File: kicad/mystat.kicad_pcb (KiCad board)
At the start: 2 copper layers, 80 x 80 mm, 66 parts, among them K1 9007-05-01, K2 9007-05-01, K3 9007-05-01, K4 9007-05-01, P1 USB Terminal, P2 CELL, P3 ICSP, U1 LM2662, U2 PIC16F1459, U3 ADR421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

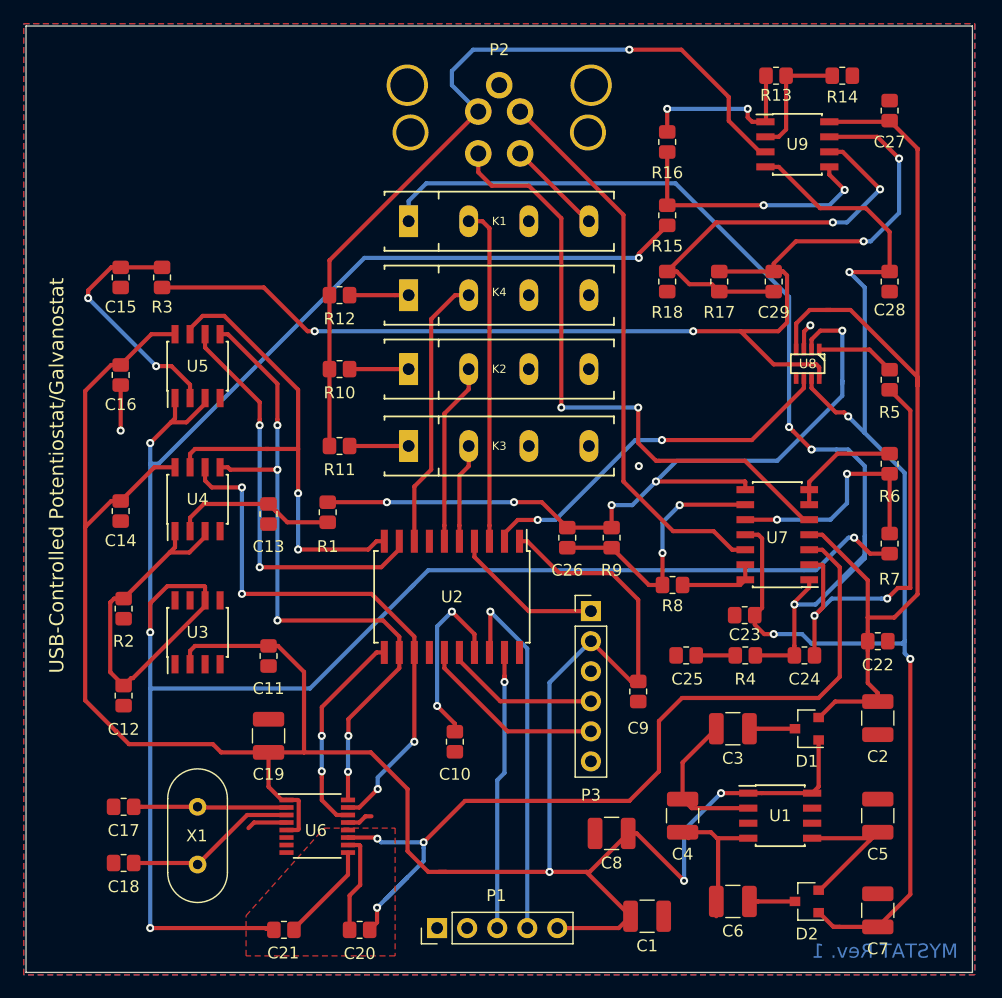
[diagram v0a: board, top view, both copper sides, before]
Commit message: Add files via upload
Modified PCB layout.  Made overall PCB dimensions smaller to fit the chosen case, all traces were made as wide as possible, changed relative position of all components in an attempt to minimize overall trace length.
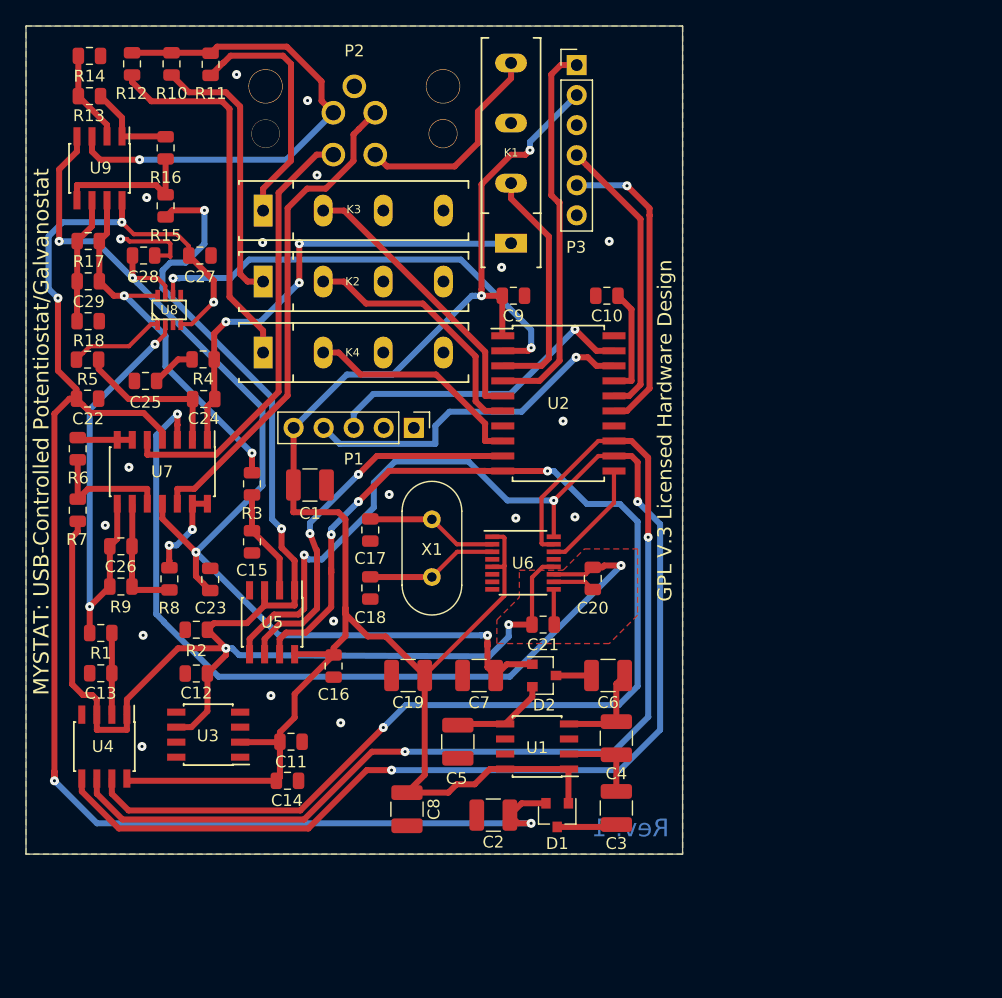
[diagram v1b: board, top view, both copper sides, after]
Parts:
- moved C22 69.9 mm to (55.2, 81.5)
- moved R7 68.7 mm to (54.4, 90.9)
- moved R6 68.6 mm to (54.4, 85.7)
- moved R5 67.8 mm to (55.2, 78.2), turned to 180 degrees
- moved R14 63.7 mm to (55.4, 52.5)
- moved C28 63.1 mm to (59.9, 69.4), turned to 0 degrees
- moved C27 59.6 mm to (64.7, 69.4), turned to 180 degrees
- moved U9 59.0 mm to (56.2, 62.0), turned to 270 degrees
- moved R13 58.1 mm to (55.4, 55.9), turned to 0 degrees
- moved C29 57.9 mm to (55.3, 71.6), turned to 0 degrees
- moved C24 55.2 mm to (65.0, 81.5), turned to 180 degrees
- moved U8 54.2 mm to (62.1, 74.0), turned to 90 degrees
- moved R17 53.4 mm to (55.3, 68.2), turned to 0 degrees
- moved U7 52.3 mm to (61.5, 87.7), turned to 270 degrees
- moved R4 52.2 mm to (65.0, 78.2)
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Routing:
- net /VREF: track 220.4 -> 134.4 mm, vias 5 -> 4
- net /SCK: track 58.0 -> 128.9 mm, vias 5 -> 4
- net /I_MEAS: track 97.6 -> 32.0 mm, vias 4 -> 2
- net /CS2: track 44.4 -> 108.0 mm, vias 2 -> 4
- net +5V: track 215.6 -> 157.2 mm, vias 3 -> 2
- net Net-(C24-Pad1): track 87.7 -> 39.5 mm
- net /SDIO: track 46.8 -> 90.8 mm, vias 4 -> 2
- net +9V: track 90.3 -> 129.8 mm, vias 0 -> 5
- net /V_MEAS: track 67.9 -> 38.4 mm, vias 5 -> 2
- net Net-(K4-Pad1): track 4.99 -> 31.6 mm
- net /CE: track 69.8 -> 44.2 mm
- net Net-(C29-Pad1): track 36.2 -> 10.7 mm, vias 2 -> 0
- net Net-(C24-Pad2): track 35.6 -> 13.3 mm, vias 2 -> 0
- net /MCLR: track 13.1 -> 32.5 mm
- net Net-(K2-Pad1): track 4.99 -> 23.3 mm
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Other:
- board size 80 x 80 mm -> 55.5 x 70 mm
- net class Default: clearance 0.2286 -> 0.254; trace_width 0.2286 -> 0.508; via_dia 0.6858 -> 0.762; via_drill 0.3302 -> 0.254
- net class power removed
- rule trace_clearance: 0.2286 -> 0.254
- board text added: "GPL V.3 Licensed Hardware Design"
- board text added: "MYSTAT: USB-Controlled Potentiostat/Galvanostat"
- board text added: "Rev. 1"
- board text removed: "MYSTAT Rev. 1"
- board text removed: "USB-Controlled Potentiostat/Galvanostat"

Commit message: Add files via upload
Corrected PCB trace routing to provide more direct ground return paths.
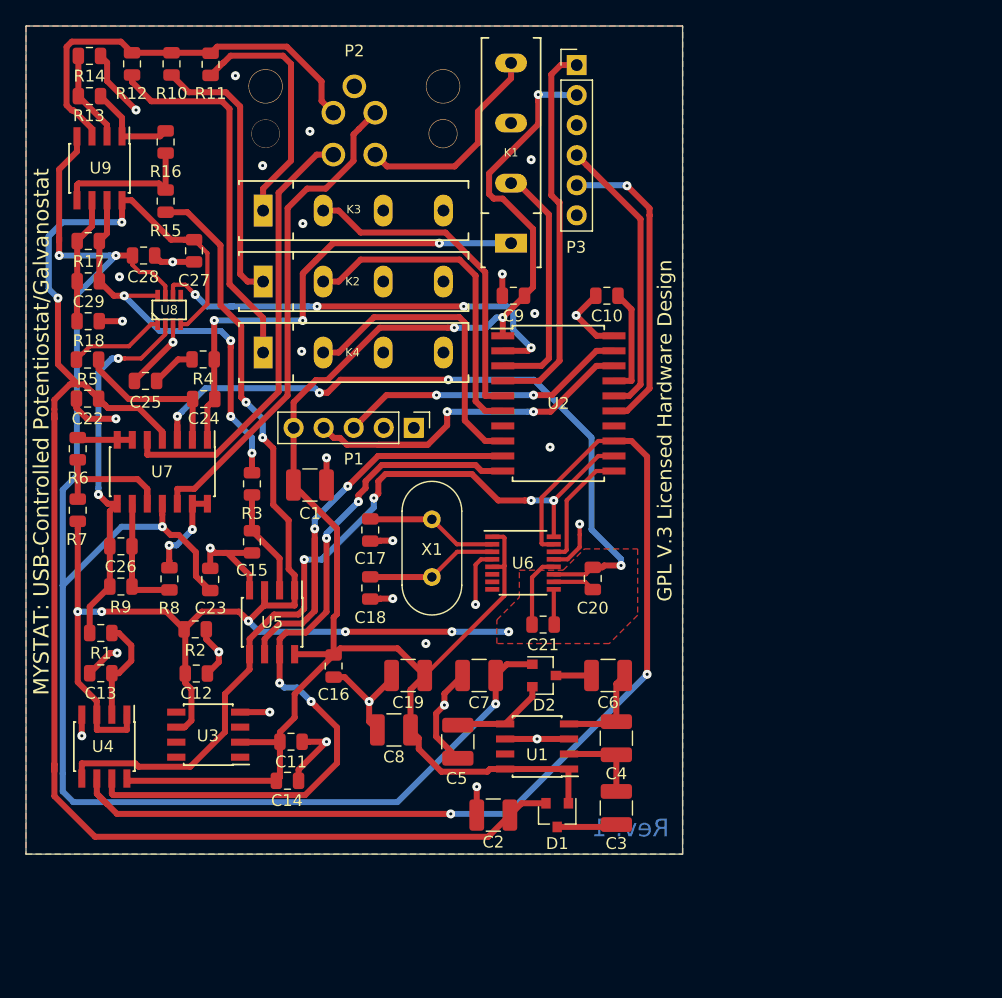
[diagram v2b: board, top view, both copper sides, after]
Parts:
- moved C8 6.79 mm to (81.1, 109.5), turned to 180 degrees
- moved C27 0.64 mm to (64.2, 69.0), turned to 90 degrees
- moved R16 0.50 mm to (61.8, 59.8)
- moved R15 0.40 mm to (61.8, 64.8)
- moved R2 0.10 mm to (64.3, 101.0), turned to 0 degrees
- turned C12 to 0 degrees
- turned C22 to 0 degrees
- turned C9 to 180 degrees
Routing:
- net GND: track 6.83 -> 99.6 mm, vias 19 -> 32
- net /SCK: track 128.9 -> 69.5 mm
- net /CS2: track 108.0 -> 64.3 mm
- net -9V: track 96.9 -> 135.7 mm
- net Net-(C20-Pad2): track 71.3 -> 59.7 mm, vias 2 -> 4
- net /VREF: track 134.4 -> 124.0 mm, vias 4 -> 8
- net /CE: track 44.2 -> 35.2 mm, vias 1 -> 0
- net /RANGE3: track 19.7 -> 26.1 mm
- net /V_MEAS: track 38.4 -> 32.0 mm
- net /SDIO2: track 33.2 -> 39.2 mm
- net /RANGE1: track 21.9 -> 27.5 mm
- net Net-(C24-Pad1): track 39.5 -> 44.1 mm
- net /RANGE2: track 23.9 -> 27.8 mm
- net /USB_D-: track 29.3 -> 32.6 mm, vias 1 -> 2
- net +5V: track 157.2 -> 154.0 mm, vias 2 -> 3
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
